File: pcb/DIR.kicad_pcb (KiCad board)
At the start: 2 copper layers, 76.2 x 50.8 mm, 125 parts, among them J1 USB_C_Receptacle, J2 Conn_01x02_Pin, J3 Conn_01x04_Socket, J4 Conn_01x07_Pin, J5 Screw_Terminal_01x02, J6 Conn_Coaxial, Q1 BSP613, Q2 AO3416A, SW1 SW_SPDT, SW2 SW_DIP_x02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

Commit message: Change Z-Diode to 3V3
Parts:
- D2: value BZV55B5V6 -> BZV33B3V3
- moved FID4 37.7 mm to (153.0, 87.6)
- moved R22 17.1 mm to (154.9, 93.5), turned to -90 degrees
- moved R18 16.1 mm to (172.7, 98.5), turned to -90 degrees
- moved R25 15.5 mm to (189.8, 84.3)
- moved D9 10.9 mm to (190.2, 84.3), turned to 0 degrees
- moved R16 10.1 mm to (186.9, 96.4), turned to 0 degrees
- moved R19 9.80 mm to (170.2, 98.5), turned to -90 degrees
- moved R24 9.55 mm to (178.3, 101.5), turned to 90 degrees
- moved C11 9.49 mm to (175.4, 92.1), turned to 180 degrees
- moved JP2 9.42 mm to (185.4, 100.1), turned to -90 degrees
- moved JP1 8.65 mm to (185.4, 92.5), turned to 90 degrees
- moved J3 7.60 mm to (184.1, 87.4), turned to -90 degrees
- moved U3 3.18 mm to (179.3, 96.4), turned to 180 degrees
- moved C7 2.95 mm to (177.2, 106.4), turned to -90 degrees
- moved Q2 2.84 mm to (188.8, 88.2)
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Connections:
- JP1 pad 1: GND -> Net-(JP1-A)
- JP1 pad 3: Net-(JP1-B) -> GND
- JP2 pad 1: Net-(JP1-B) -> Net-(JP1-A)
- R16 pad 1: Net-(JP1-B) -> Net-(JP1-A)
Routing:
- net SDA: track 56.5 -> 65.6 mm
- net +3V3: track 129.6 -> 137.4 mm, vias 18 -> 19
- net Net-(JP1-A): track 0.00 -> 5.30 mm
- net Net-(JP1-B): track 4.43 -> 0.00 mm
- net Net-(D9-K): track 7.34 -> 2.95 mm
- net Net-(Q2-G): track 13.8 -> 10.2 mm, vias 2 -> 0
- net ~{RST}: track 62.3 -> 59.8 mm, vias 4 -> 2
- net Net-(SW3-B): track 24.4 -> 22.2 mm
- net Net-(JP1-C): track 4.75 -> 6.25 mm
- net Net-(U4-PA1): track 10.7 -> 9.36 mm
- net Net-(JP2-C): track 4.74 -> 6.00 mm
- net Net-(SW4-B): track 16.2 -> 15.0 mm
- net ~{MUTE}: track 45.8 -> 44.9 mm
- net Net-(U5-RXD): track 41.9 -> 41.2 mm
- net VBUS: track 52.7 -> 52.0 mm
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
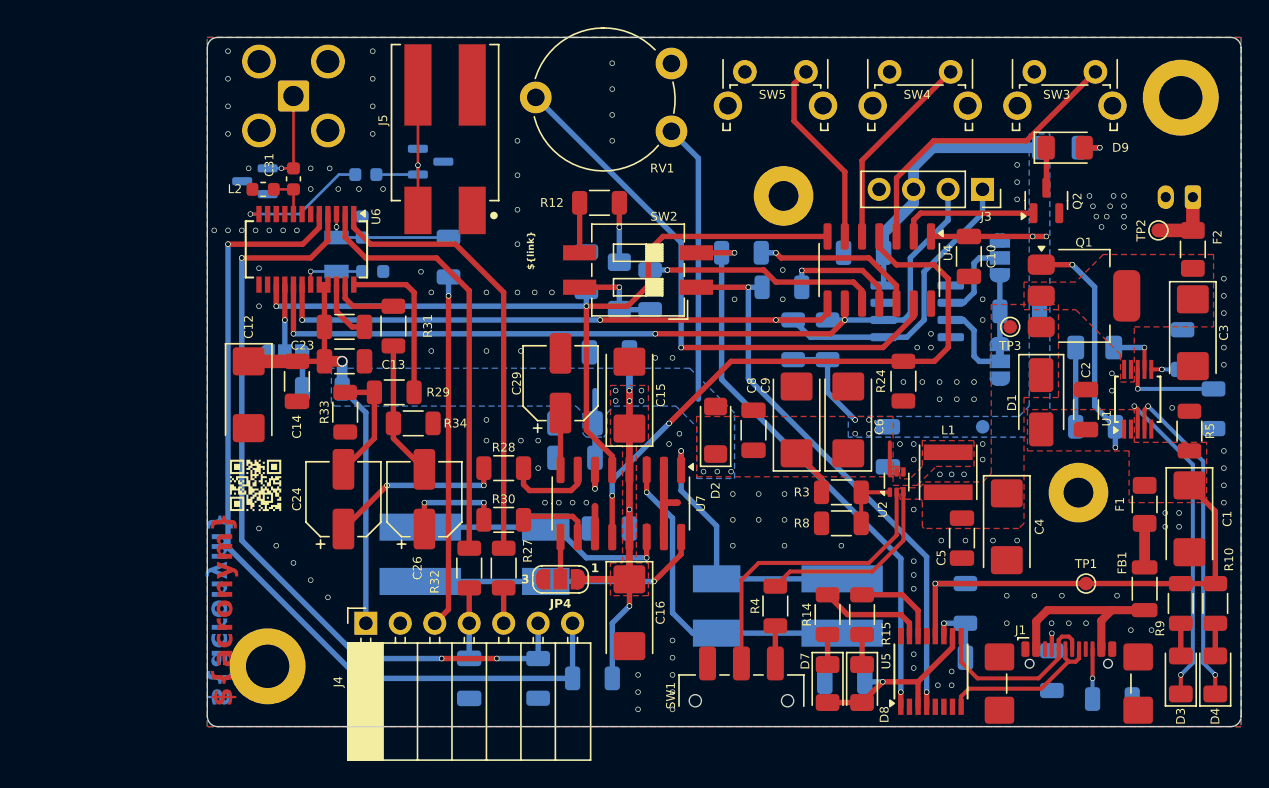
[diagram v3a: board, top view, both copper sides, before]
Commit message: Fix power path issue
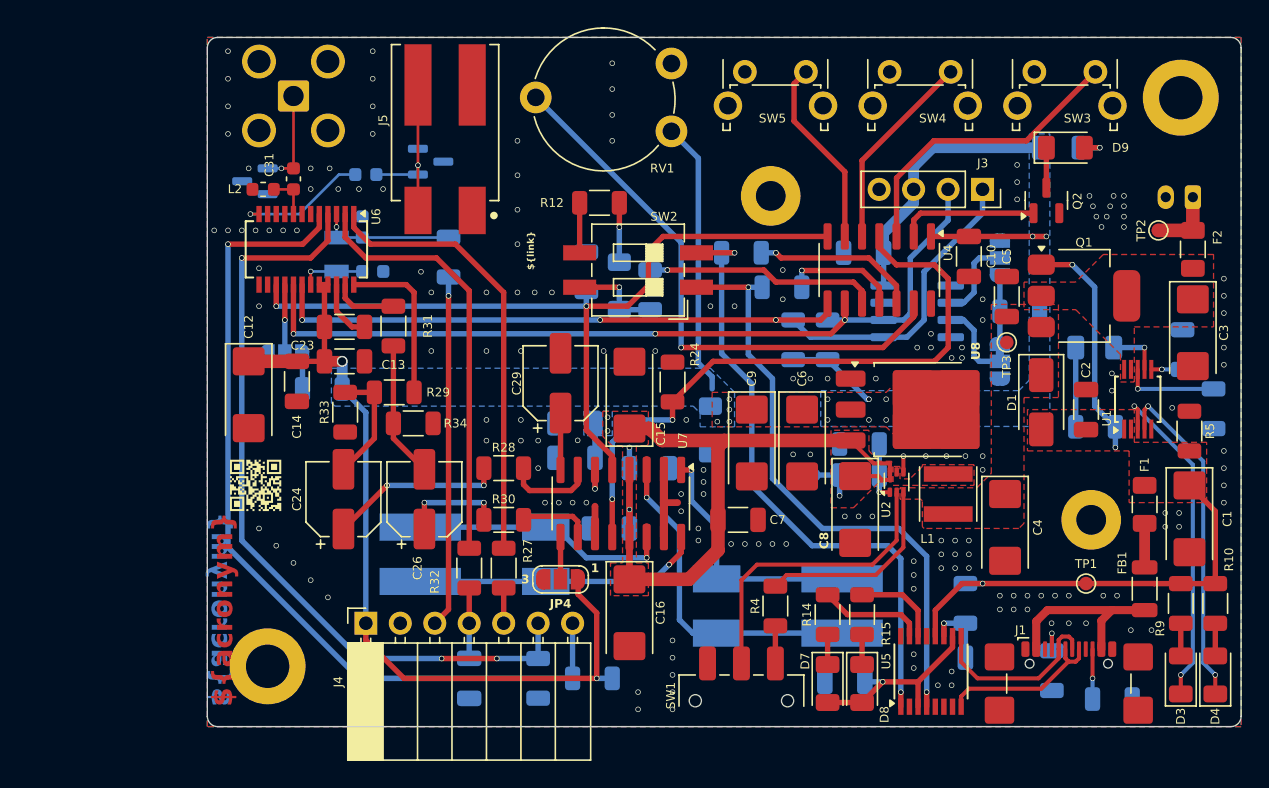
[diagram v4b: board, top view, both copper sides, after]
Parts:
- added U8: LM1117DT-3.3, Package_TO_SOT_SMD:TO-252-3_TabPin2, F.Cu at (179.5, 103.6)
- C7: moved to F.Cu
- C8: value 100n -> 10u; footprint Capacitor_SMD:C_1206_3216Metric -> Capacitor_Tantalum_SMD:CP_EIA-6032-28_Kemet-C
- D2: value BZV33B3V3 -> BZV36B3V6; moved to B.Cu
- R3: value 680k -> 732k; moved to B.Cu
- R8: value 150k -> 100k; moved to B.Cu
- moved C5 18.1 mm to (185.9, 95.3), turned to 90 degrees
- moved R24 17.0 mm to (161.3, 101.6), turned to -90 degrees
- moved TP4 12.9 mm to (171.7, 108.5)
- moved C7 12.3 mm to (166.1, 111.8), turned to 0 degrees
- moved C8 9.50 mm to (174.8, 111.0), turned to -90 degrees
- moved C19 9.03 mm to (159.6, 108.0), turned to 0 degrees
- moved R8 5.99 mm to (175.1, 106.2)
- moved C6 3.80 mm to (170.8, 106.1), turned to -90 degrees
- moved C9 3.71 mm to (167.1, 106.1), turned to -90 degrees
- moved H4 2.22 mm to (192.2, 111.8)
- moved FID2 2.07 mm to (185.4, 111.1)
- moved R3 1.84 mm to (175.1, 108.5)
- moved L1 1.60 mm to (181.6, 109.9)
- moved TP3 1.17 mm to (185.9, 98.7)
- moved H3 0.95 mm to (168.5, 87.9)
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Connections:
- C15 pad 1: +3V3 -> +5V
- C16 pad 1: +3V3 -> +5V
- C17 pad 1: +3V3 -> +5V
- C18 pad 1: +3V3 -> +5V
- C19 pad 1: +3V3 -> +5V
- C20 pad 1: +3V3 -> +5V
- C7 pad 1: +3V3 -> +5V
- C8 pad 1: +3V3 -> +5V
- R3 pad 2: +3V3 -> +5V
- TP4 pad 1: +3V3 -> +5V
- U2 pad 6: +3V3 -> +5V
- U7 pad 13: +3V3 -> +5V
- U7 pad 4: +3V3 -> +5V
- U7 pad 6: +3V3 -> +5V
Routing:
- net +5V: track 0.00 -> 61.0 mm, vias 0 -> 6
- net +3V3: track 137.4 -> 116.7 mm, vias 19 -> 14
- net Net-(U5-RXD): track 41.2 -> 44.5 mm
- net Net-(U5-TXD): track 42.7 -> 46.0 mm
- net ~{MUTE}: track 44.9 -> 47.4 mm
- net VBUS: track 52.0 -> 49.9 mm
- net Net-(U7-+OUT_L): track 20.3 -> 18.8 mm
- net GND: track 0.01 -> 1.18 mm, vias 153 -> 169
- net Net-(U2-FB): track 4.40 -> 4.33 mm, vias 0 -> 1
- added copper zone on B.Cu, net +5V
- added copper zone on F.Cu, net +5V

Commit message: Change SHDN and MUTE pins
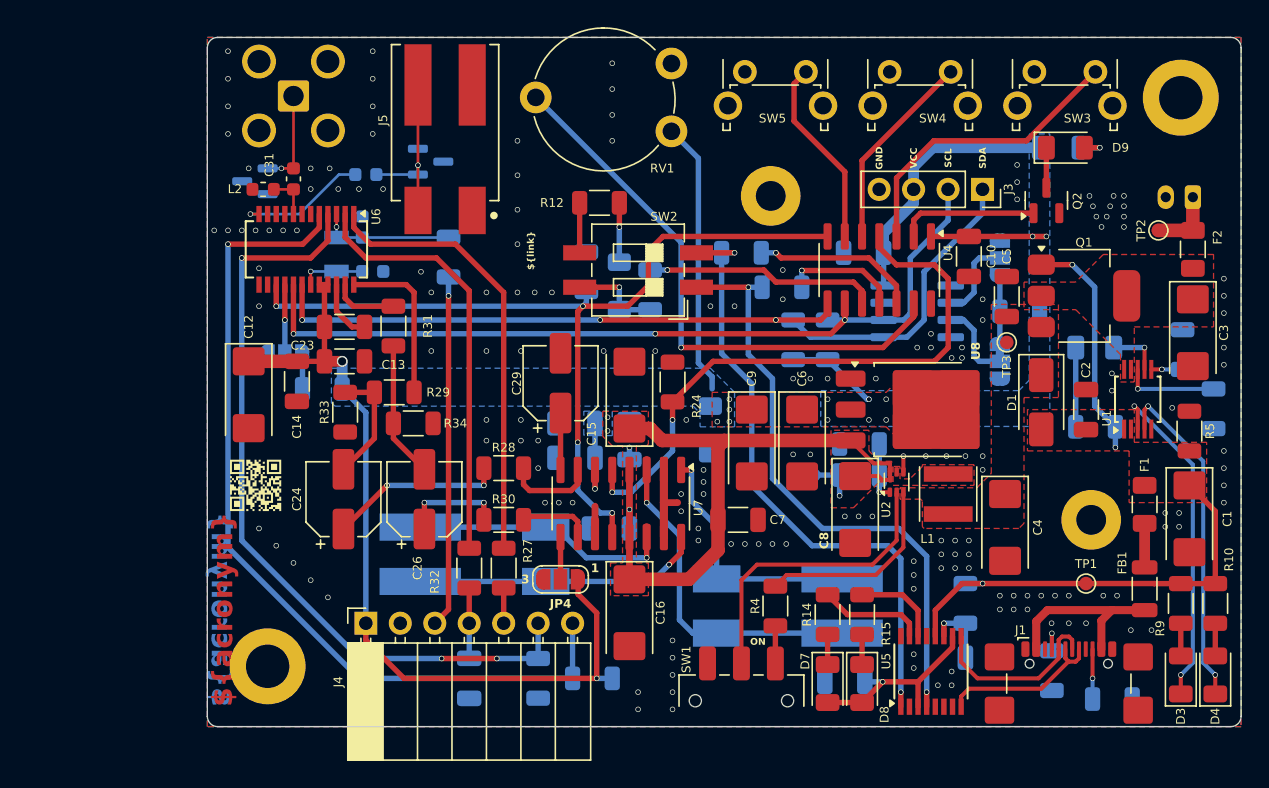
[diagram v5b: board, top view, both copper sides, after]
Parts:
- moved C19 2.57 mm to (158.1, 105.8), turned to 90 degrees
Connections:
- U7 pad 12: ~{MUTE} -> ~{RST}
- U7 pad 5: ~{RST} -> ~{MUTE}
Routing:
- net ~{RST}: track 59.8 -> 65.8 mm, vias 2 -> 4
- net ~{MUTE}: track 47.4 -> 44.9 mm
- net +5V: track 61.0 -> 60.4 mm
- net GND: vias 169 -> 167
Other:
- board text added: "+"
- board text added: "A1"
- board text added: "A2"
- board text added: "GND"
- board text added: "ON"
- board text added: "SCL"
- board text added: "SDA"
- board text added: "SEN"
- board text added: "VCC"

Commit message: Modify pcb position
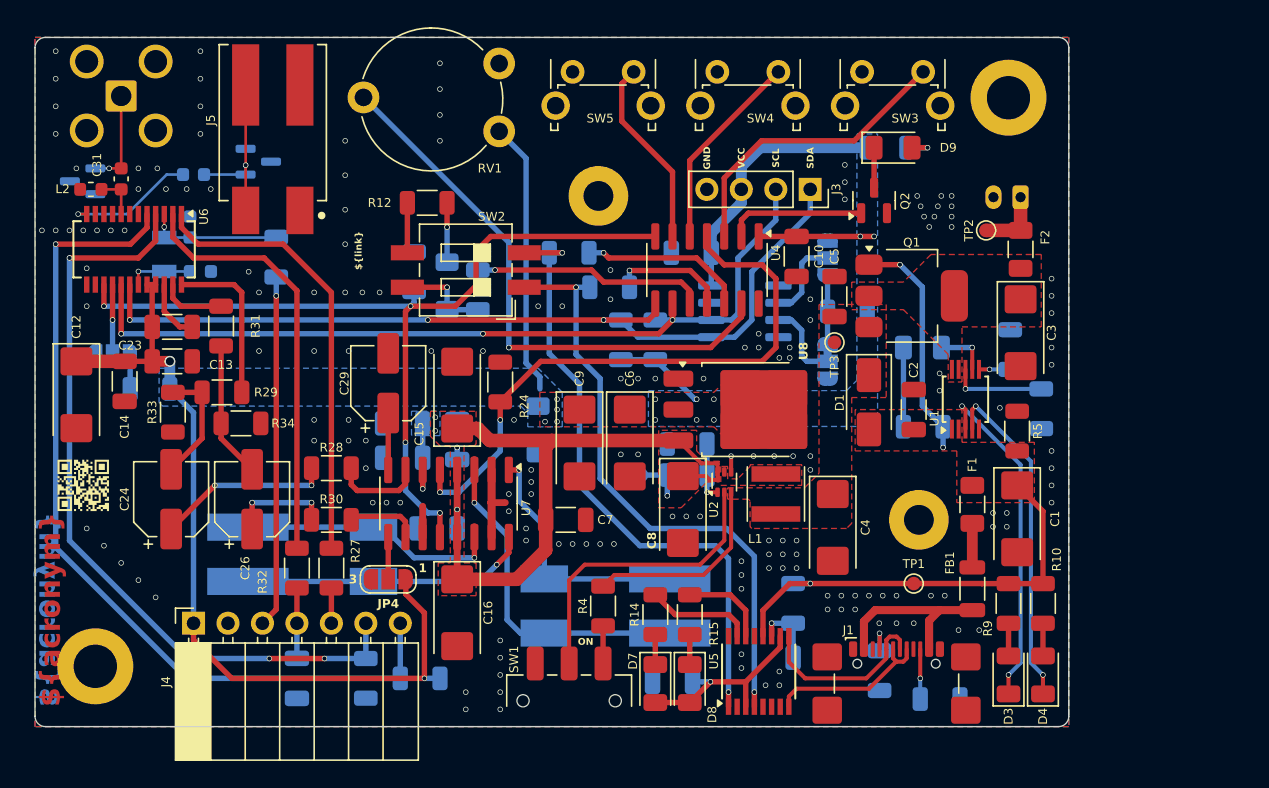
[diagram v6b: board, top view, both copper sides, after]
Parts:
- moved C14 12.7 mm to (120.9, 101.6)
- moved C15 12.7 mm to (145.4, 102.6)
- moved C16 12.7 mm to (145.4, 118.6)
- moved C19 12.7 mm to (145.4, 105.8)
- moved C2 12.7 mm to (179.1, 103.6)
- moved C21 12.7 mm to (161.3, 123.7)
- moved C26 12.7 mm to (130.3, 110.2)
- moved C3 12.7 mm to (186.9, 98.0)
- moved C7 12.7 mm to (153.4, 111.8)
- moved C8 12.7 mm to (162.1, 111.0)
- moved C9 12.7 mm to (154.4, 106.1)
- moved D10 12.7 mm to (130.8, 85.4)
- moved D2 12.7 mm to (151.4, 105.1)
- moved D6 12.7 mm to (144.7, 94.5)
- moved D9 12.7 mm to (177.5, 84.3)
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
